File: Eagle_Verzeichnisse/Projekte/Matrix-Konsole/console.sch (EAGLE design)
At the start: 12 parts, among them IC1 74HC595D, IC2 74HC595D, IC3 74HC595D

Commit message: Added MAX7219, Added Potentiometer, Made curcuit diagram clearer, Changed Connectors
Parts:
- removed IC1, IC2, IC3: 74HC595D, 74xx-eu:74HC595D
- removed X2, X3, X4, X5: (no value), con-yamaichi:MDIN05K
- added R1: 200, rcl:R-EU_0414/5V
- added R2: PC16-SHM2, piher:PC16-SHM2
- added U$2: MAX7219CWG, max7219:MAX7219CWG
- added X6, X7, X8, X9: MAB5WH, con-hirschmann:MAB5WH
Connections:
- net N$1 renamed MATRIX_G1
- net N$2 renamed MATRIX_R1
- net N$29 renamed MATRIX_B1
- net N$30 renamed MATRIX_R2
- net N$33 renamed MATRIX_A
- net N$34 renamed MATRIX_B
- net N$35 renamed MATRIX_C
- net N$36 renamed MATRIX_D
- net N$37 renamed MATRIX_LAT
- net N$38 renamed MATRIX_CLK
- net N$39 renamed MATRIX_OE
- removed net CLK1: IC4.(A14)PC6, X2.2
- removed net CLK2: IC4.(A11)PC3, X3.2
- removed net CLK3: IC4.(A8)PC0, X4.2
- removed net CLK4: IC4.PG1(!RD!), X5.2
- removed net DS: IC1.SER, IC4.(OC3B/AIN4)PE4
- removed net N$10: 7SEG2.CC4, IC1.QH
- removed net N$11: 7SEG1.A, IC2.QA
- removed net N$12: 7SEG1.B, IC2.QB
- removed net N$13: 7SEG1.C, IC2.QC
- removed net N$14: 7SEG1.D, IC2.QD
- removed net N$15: 7SEG1.E, IC2.QE
- removed net N$16: 7SEG1.F, IC2.QF
- removed net N$17: 7SEG1.G, IC2.QG
- removed net N$18: 7SEG1.DP, IC2.QH
- removed net N$19: 7SEG2.A, IC3.QA
- removed net N$20: 7SEG2.B, IC3.QB
- removed net N$21: 7SEG2.C, IC3.QC
- removed net N$22: 7SEG2.D, IC3.QD
- removed net N$23: 7SEG2.E, IC3.QE
- removed net N$24: 7SEG2.F, IC3.QF
- removed net N$25: 7SEG2.G, IC3.QG
- removed net N$26: 7SEG2.DP, IC3.QH
- removed net N$27: IC1.QH*, IC2.SER
- removed net N$28: IC2.QH*, IC3.SER
- removed net N$3: 7SEG1.CC1, IC1.QA
- removed net N$31: IC4.(AD6)PA6, U$1.B2
- removed net N$32: IC4.(AD7)PA7, U$1.G2
- removed net N$4: 7SEG1.CC2, IC1.QB
- removed net N$5: 7SEG1.CC3, IC1.QC
- removed net N$6: 7SEG1.CC4, IC1.QD
- removed net N$7: 7SEG2.CC1, IC1.QE
- removed net N$8: 7SEG2.CC2, IC1.QF
- removed net N$9: 7SEG2.CC3, IC1.QG
- removed net SHCP: IC1.SCK, IC2.SCK, IC3.SCK, IC4.(OC3C/INT5)PE5
- removed net STCP: IC1.RCK, IC2.RCK, IC3.RCK, IC4.PG5(OC0B)
- new net A: 7SEG1.A, U$2.SEGA
- new net B: 7SEG1.B, 7SEG2.B, U$2.SEGB
- new net C: 7SEG1.C, 7SEG2.C, U$2.SEGC
- new net CLK: IC4.(A14)PC6, X6.2, X7.2, X8.2, X9.2
- new net D: 7SEG1.D, 7SEG2.D, U$2.SEGD
- new net DIG0: 7SEG1.CC1, U$2.DIG0
- new net DIG1: 7SEG1.CC2, U$2.DIG1
- new net DIG2: 7SEG1.CC3, U$2.DIG2
- new net DIG3: 7SEG1.CC4, U$2.DIG3
- new net DIG4: 7SEG2.CC1, U$2.DIG4
- new net DIG5: 7SEG2.CC2, U$2.DIG5
- new net DIG6: 7SEG2.CC3, U$2.DIG6
- new net DIG7: 7SEG2.CC4, U$2.DIG7
- new net DP: 7SEG1.DP, 7SEG2.DP, U$2.SEGDP
- new net E: 7SEG1.E, 7SEG2.E, U$2.SEGE
- new net F: 7SEG1.F, 7SEG2.F, U$2.SEGF
- new net G: 7SEG1.G, 7SEG2.G, U$2.SEGG
- new net MATRIX_B2: IC4.(AD7)PA7, U$1.B2
- new net MATRIX_G2: IC4.(AD6)PA6, U$1.G2
- new net MAX_CLK: IC4.(OC3C/INT5)PE5, U$2.CLK
- new net MAX_DIN: IC4.(OC3B/AIN4)PE4, U$2.DIN
- new net MAX_ISET: R1.1, U$2.ISET
- new net MAX_LOAD: IC4.PG5(OC0B), U$2.LOAD
- new net N$1: IC4.PK1(ADC9/PCINT17), R2G$1.1S
- new net N$2: 7SEG2.A
- net GND: now also R2G$1.1E, U$2.GND@1, U$2.GND@2, X6.5, X7.5, X8.5, X9.5; no longer IC1.GND, IC2.GND, IC3.GND, X2.5, X3.5, X4.5, X5.5
- net PL: now also X6.1, X7.1, X8.1, X9.1; no longer X2.1, X3.1, X4.1, X5.1
- net SER1: now also X6.3; no longer X2.3
- net SER2: now also X7.3; no longer X3.3
- net SER3: now also X8.3; no longer X4.3
- net SER4: now also X9.3; no longer X5.3
- net VCC: now also R1.2, R2G$1.1A, U$2.VCC, X6.4, X7.4, X8.4, X9.4; no longer IC1.G, IC1.SCL, IC1.VCC, IC2.G, IC2.SCL, IC2.VCC, IC3.G, IC3.SCL, IC3.VCC, X2.4, X3.4, X4.4, X5.4
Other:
- moved on the sheet: 7SEG1, 7SEG2

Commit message: Added Board to console, Added Pin header
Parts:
- removed X6, X7, X8, X9: MAB5WH, con-hirschmann:MAB5WH
- added J1, J2, J3, J4: DIN5, SparkFun-Connectors:DIN5
- added JP1: (no value), pinhead:PINHD-1X24
- added X2: 057-016-1, con-panduit:057-016-1
- R1: device rcl:R-EU_0414/5V -> resistor:R-EU_M3516
- renumbered IC4 to IC1
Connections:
- net CLK: now also J1.2, J2.2, J3.2, J4.2, JP1.12; no longer X6.2, X7.2, X8.2, X9.2
- net GND: now also J1.5, J2.5, J3.5, J4.5, JP1.24, X2-16.S, X2-4.S, X2-8.S; no longer X6.5, X7.5, X8.5, X9.5
- net MATRIX_A: now also JP1.4, X2-9.S
- net MATRIX_B: now also JP1.5, X2-10.S
- net MATRIX_B1: now also JP1.20, X2-3.S
- net MATRIX_B2: now also JP1.17, X2-7.S
- net MATRIX_C: now also JP1.6, X2-11.S
- net MATRIX_CLK: now also JP1.15, X2-13.S
- net MATRIX_D: now also JP1.7, X2-12.S
- net MATRIX_G1: now also JP1.21, X2-2.S
- net MATRIX_G2: now also JP1.18, X2-6.S
- net MATRIX_LAT: now also JP1.16, X2-14.S
- net MATRIX_OE: now also JP1.1, X2-15.S
- net MATRIX_R1: now also JP1.22, X2-1.S
- net MATRIX_R2: now also JP1.19, X2-5.S
- net MAX_CLK: now also JP1.8
- net MAX_DIN: now also JP1.9
- net MAX_LOAD: now also JP1.3
- net PL: now also J1.1, J2.1, J3.1, J4.1, JP1.11; no longer X6.1, X7.1, X8.1, X9.1
- net SER1: now also J4.3, JP1.13; no longer X6.3
- net SER2: now also J3.3, JP1.14; no longer X7.3
- net SER3: now also J2.3, JP1.10; no longer X8.3
- net SER4: now also J1.3, JP1.2; no longer X9.3
- net VCC: now also J1.4, J2.4, J3.4, J4.4, JP1.23; no longer X6.4, X7.4, X8.4, X9.4
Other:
- moved on the sheet: X1-1, X1-2

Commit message: Added Z-Diode
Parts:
- added D1: 5V, diode:ZENER-DIODEDO35Z10
- added JP2: (no value), pinhead:PINHD-1X4
- added R3: 2,7, resistor:R-EU_M3516
- JP1: device pinhead:PINHD-1X24 -> pinhead:PINHD-1X25
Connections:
- removed net N$1: IC1.PK1(ADC9/PCINT17), R2G$1.1S
- removed net N$2: 7SEG2.A
- new net 5V: IC1.!RESET, IC1.+5V@2, J1.4, J2.4, J3.4, J4.4, JP1.24, R1.2, R2G$1.1A, U$2.VCC
- new net MEGA_A9: IC1.PK1(ADC9/PCINT17), JP1.23, R2G$1.1S
- new net MEGA_GND: IC1.GND@1, J1.5, J2.5, J3.5, J4.5, JP1.25, R2G$1.1E, U$1.GND1, U$1.GND2, U$1.GND3, U$2.GND@1, U$2.GND@2, X2-16.S, X2-4.S, X2-8.S
- new net N$3: D1.C, JP2.1, JP2.2, R3.1, U$1.VCC
- net A: now also 7SEG2.A
- net GND: now also D1.A, JP2.3, JP2.4, U$1.GND4; no longer IC1.GND@1, IC1.GND@2, IC1.GND@3, IC1.GND@4, IC1.GND@5, J1.5, J2.5, J3.5, J4.5, JP1.24, R2G$1.1E, U$1.GND1, U$1.GND2, U$1.GND3, U$2.GND@1, U$2.GND@2, X2-16.S, X2-4.S, X2-8.S
- net VCC: now also R3.2; no longer IC1.!RESET, IC1.+5V@1, IC1.+5V@2, IC1.+5V@3, J1.4, J2.4, J3.4, J4.4, JP1.23, R1.2, R2G$1.1A, U$2.VCC
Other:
- moved on the sheet: 7SEG1, 7SEG2, J1, J2, J3, J4

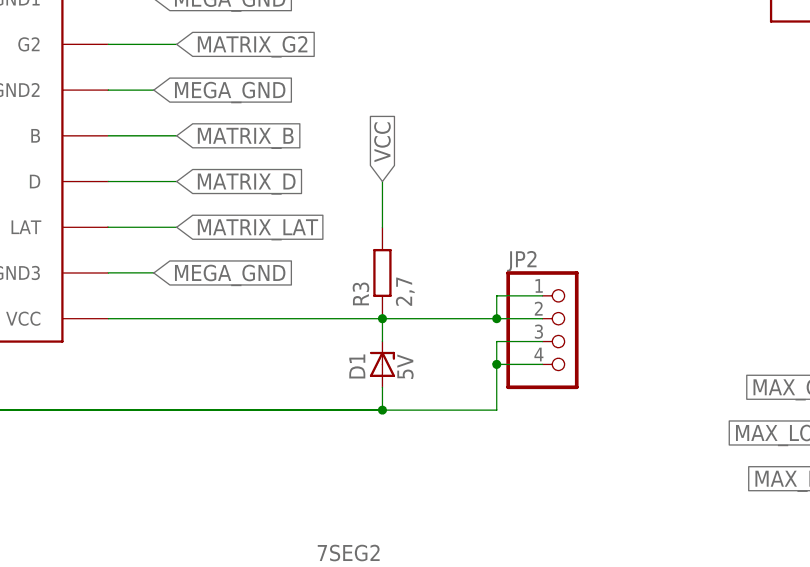
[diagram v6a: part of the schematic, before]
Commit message: Changed z-Diode-resistor to 10 Ohm
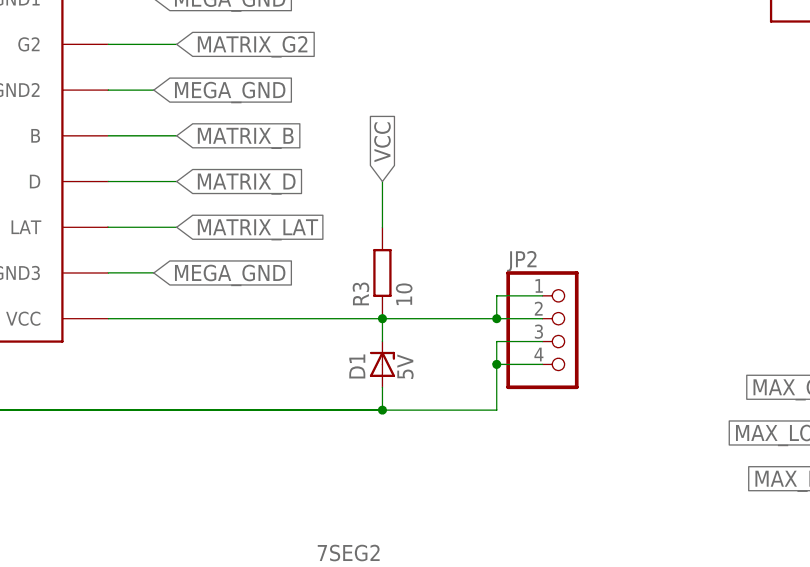
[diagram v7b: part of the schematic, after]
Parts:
- R3: value 2,7 -> 10
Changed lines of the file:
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@@
 <?xml version="1.0" encoding="utf-8"?>
 <!DOCTYPE eagle SYSTEM "eagle.dtd">
-<eagle version="8.1.0">
+<eagle version="8.0.2">
 <drawing>
 <settings>
@@
 <setting verticaltext="up"/>
 </settings>
-<grid distance="0.1" unitdist="inch" unit="inch" style="lines" multiple="1" display="yes" altdistance="0.01" altunitdist="inch" altunit="inch"/>
+<grid distance="0.1" unitdist="inch" unit="inch" style="lines" multiple="1" display="no" altdistance="0.01" altunitdist="inch" altunit="inch"/>
 <layers>
 <layer number="1" name="Top" color="4" fill="1" visible="no" active="no"/>
@@
 <part name="U$1" library="Matrix" deviceset="32X32MATRIX_DEV" device=""/>
 <part name="JP2" library="pinhead" deviceset="PINHD-1X4" device=""/>
-<part name="R3" library="resistor" deviceset="R-EU_" device="M3516" value="2,7"/>
+<part name="R3" library="resistor" deviceset="R-EU_" device="M3516" value="10"/>
 <part name="GND13" library="supply1" deviceset="GND" device=""/>
 <part name="D1" library="diode" deviceset="ZENER-DIODE" device="DO35Z10" value="5V"/>
